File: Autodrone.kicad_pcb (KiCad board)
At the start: 4 copper layers, 37.1 x 37.2 mm, 124 parts, among them J1 Conn_01x02, J10 Conn_01x08, J11 Conn_01x03, J12 Conn_01x02, J13 USB_B_Micro, J14 Conn_01x04, J15 Conn_01x04, J16 Conn_01x01, J17 Conn_01x04, J2 Conn_01x04, J3 Conn_01x04, J4 Conn_01x03, J5 Conn_01x03, J6 Conn_01x06, J7 Conn_01x06, J8 Conn_01x04, J9 Conn_01x08, Q1 BSS138, SW1 SW_Push, U1 LP2985-3.3, U10 W25Q128JVS, U2 STM32F722RETx, U3 LP2985-3.3, U4 MP4560_QFN10, U5 MP4560_QFN10, U6 MAX7456EUI+, U7 MPU-6000, U9 BMP388, Y1 27MHz

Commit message: Lots of changes made
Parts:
- removed the C1 at (89.8, 92.0)
- removed the C16 at (89.9, 96.8)
- removed the C2 at (88.0, 96.8)
- removed the C23 at (83.3, 102.5)
- removed the C39 at (108.8, 84.1)
- removed the C40 at (100.6, 78.7)
- removed the C41 at (108.8, 82.1)
- removed the C42 at (108.8, 85.1)
- removed the C43 at (99.2, 79.6)
- removed the C44 at (97.4, 83.9)
- removed the C45 at (105.6, 94.2)
- removed the C46 at (103.0, 89.4)
- removed the D3 at (97.8, 104.8)
- removed the FB3 at (98.7, 85.3)
- removed HSE1: 8MHz, Oscillator:Oscillator_SMD_Abracon_ASE-4Pin_3.2x2.5mm
- removed the J10 at (113.2, 95.3)
- removed the J14 at (80.0, 83.7)
- removed the J2 at (104.3, 105.0)
- removed the J6 at (83.5, 92.7)
- removed the J8 at (90.1, 108.2)
- removed the L5 at (96.6, 93.4)
- removed the R21 at (97.8, 102.3)
- removed the R22 at (96.6, 98.4)
- removed the R23 at (99.3, 102.3)
- removed the R25 at (108.8, 86.1)
- removed the R26 at (96.3, 102.3)
- removed the R29 at (108.8, 87.0)
- removed the R30 at (108.8, 88.0)
- removed the R9 at (93.4, 102.3)
- added C11: 1pF, Capacitor_SMD:C_0402_1005Metric, B.Cu at (74.0, 84.5)
- added C13: 10uF, Capacitor_SMD:C_0402_1005Metric, B.Cu at (84.5, 96.2)
- added C14: 10uF, Capacitor_SMD:C_0402_1005Metric, B.Cu at (84.1, 86.5)
- added C17: 2.2uF, Capacitor_SMD:C_0402_1005Metric, F.Cu at (97.2, 87.5)
- added C20: 0.1uF, Capacitor_SMD:C_0402_1005Metric, F.Cu at (97.8, 94.6)
- added C21: 0.1uF, Capacitor_SMD:C_0402_1005Metric, F.Cu at (97.5, 90.7)
- added C22: 0.1uF, Capacitor_SMD:C_0402_1005Metric, F.Cu at (99.4, 88.8)
- added C25: 0.01uF, Capacitor_SMD:C_0402_1005Metric, B.Cu at (115.3, 88.5)
- added C27: 0.01uF, Capacitor_SMD:C_0402_1005Metric, B.Cu at (121.3, 89.9)
- added C28: 0.022uF, Capacitor_SMD:C_0402_1005Metric, B.Cu at (113.9, 91.1)
- added C29: 0.47uF, Capacitor_SMD:C_0402_1005Metric, B.Cu at (120.1, 92.1)
- added C3: 33uF, Capacitor_SMD:C_0402_1005Metric, B.Cu at (78.6, 100.0)
- added C30: 0.22uF, Capacitor_SMD:C_0402_1005Metric, B.Cu at (113.9, 89.2)
- added C31: 10uF, Capacitor_SMD:C_0402_1005Metric, F.Cu at (105.3, 82.7)
- added C33: 0.1uF, Capacitor_SMD:C_0402_1005Metric, F.Cu at (109.0, 82.2)
- added C34: 0.1uF, Capacitor_SMD:C_0402_1005Metric, F.Cu at (104.1, 90.4)
- added C36: 0.1uF, Capacitor_SMD:C_0402_1005Metric, F.Cu at (111.2, 82.2)
- added D10: YELLOW, LED_SMD:LED_0603_1608Metric, F.Cu at (74.0, 105.2)
- added D11: GREEN, LED_SMD:LED_0603_1608Metric, F.Cu at (72.6, 79.0)
- added D12: GREEN, LED_SMD:LED_0603_1608Metric, F.Cu at (72.9, 104.2)
- added D13: PURPLE, LED_SMD:LED_0603_1608Metric, F.Cu at (71.9, 103.1)
- added D6: BLUE, LED_SMD:LED_0603_1608Metric, F.Cu at (76.0, 107.3)
- added FB2: 100 @ 100 Mhz, Inductor_SMD:L_0603_1608Metric, F.Cu at (102.8, 84.5)
- added G***: LOGO, Footprints:LED, F.Cu at (76.8, 80.1)
- added G***: LOGO, Footprints:LED, F.Cu at (78.3, 102.1)
- added J1: Conn_01x03, Connector_Wire:SolderWire-0.1sqmm_1x03_P3.6mm_D0.4mm_OD1mm, F.Cu at (105.2, 78.5)
- added J11: Conn_01x02, Connector_Wire:SolderWire-0.75sqmm_1x02_P4.8mm_D1.25mm_OD2.3mm, F.Cu at (120.1, 105.7)
- added J15: Conn_01x04, Connector_Wire:SolderWire-0.1sqmm_1x04_P3.6mm_D0.4mm_OD1mm, F.Cu at (94.2, 104.7)
- added J3: Conn_01x08, Connector_JST:JST_SH_SM08B-SRSS-TB_1x08-1MP_P1.00mm_Horizontal, F.Cu at (118.8, 91.6)
- added J4: Conn_01x08, Connector_Wire:SolderWire-0.1sqmm_1x08_D0.4mm_OD1mm, F.Cu at (123.3, 91.6)
- added JP1: SolderJumper_2_Open, Jumper:SolderJumper-2_P1.3mm_Open_TrianglePad1.0x1.5mm, B.Cu at (104.4, 101.5)
- added JP2: SolderJumper_2_Open, Jumper:SolderJumper-2_P1.3mm_Open_TrianglePad1.0x1.5mm, B.Cu at (106.9, 101.5)
- added L3: Arrow, Footprints:Arrow, F.Cu at (104.3, 95.4)
- added R11: 67k, Resistor_SMD:R_0402_1005Metric, B.Cu at (118.5, 94.7)
- added R12: 75k, Resistor_SMD:R_0402_1005Metric, B.Cu at (120.1, 94.2)
- added R13: 10k, Resistor_SMD:R_0402_1005Metric, B.Cu at (121.3, 92.1)
- added R14: 1k, Resistor_SMD:R_0402_1005Metric, F.Cu at (112.3, 82.2)
- added R15: 1k, Resistor_SMD:R_0402_1005Metric, F.Cu at (113.4, 82.2)
- added R16: 1k, Resistor_SMD:R_0402_1005Metric, F.Cu at (112.9, 91.3)
- added R17: 75, Resistor_SMD:R_0402_1005Metric, F.Cu at (105.3, 81.7)
- added R18: 75, Resistor_SMD:R_0402_1005Metric, F.Cu at (110.1, 82.2)
- added R19: 589, Resistor_SMD:R_0402_1005Metric, F.Cu at (109.4, 92.3)
- added R27: 1k, Resistor_SMD:R_0402_1005Metric, B.Cu at (76.1, 76.3)
- added R31: 1k, Resistor_SMD:R_0402_1005Metric, B.Cu at (75.1, 77.4)
- added R32: 1k, Resistor_SMD:R_0402_1005Metric, B.Cu at (75.4, 105.8)
- added R36: 1k, Resistor_SMD:R_0402_1005Metric, B.Cu at (73.3, 103.8)
- added R37: 1k, Resistor_SMD:R_0402_1005Metric, B.Cu at (72.3, 102.7)
- added R8: 147k, Resistor_SMD:R_0402_1005Metric, B.Cu at (74.0, 86.8)
- added U2: MP4462, Package_DFN_QFN:DFN-10-1EP_3x3mm_P0.5mm_EP1.7x2.5mm, B.Cu at (77.0, 85.5)
- added U8: DRV8424E, Package_DFN_QFN:VQFN-24-1EP_4x4mm_P0.5mm_EP2.45x2.45mm, B.Cu at (117.0, 91.6)
- added Y2: CSTNE8M00G55Z000R0, Footprints:OSC_CSTNE8M00G55Z000R0, B.Cu at (98.7, 83.1)
- C10: renamed from C34; value 390pF -> 330pF
- C19: value 2.2uF -> 0.1uF
- C26: value 10pF -> 100uF
- C32: value 10pF -> 10uF; moved to F.Cu
- C35: value 1pF -> 0.1uF; moved to F.Cu
- C37, C38: value 10uF -> 10pF
- C4: renamed from C22; footprint Capacitor_SMD:C_0603_1608Metric -> Capacitor_SMD:C_0402_1005Metric
- C47: renamed from C15; moved to B.Cu
- C5: renamed from C29; footprint Capacitor_SMD:C_0603_1608Metric -> Capacitor_SMD:C_0402_1005Metric
- C7: renamed from C24; footprint Capacitor_SMD:C_0603_1608Metric -> Capacitor_SMD:C_0402_1005Metric
- C9: renamed from C33; value 390pF -> 330pF
- D3: renamed from D1; moved to B.Cu
- D7: value YELLOW -> RED
- D8: value GREEN -> RED
- D9: value PURPLE -> YELLOW
- FB1: moved to B.Cu
- J16: moved to F.Cu
- J17: value Conn_01x04 -> Conn_01x01; footprint Connector_Wire:SolderWire-0.1sqmm_1x04_P3.6mm_D0.4mm_OD1mm -> Connector_Wire:SolderWire-0.1sqmm_1x01_D0.4mm_OD1mm
- J5: value Conn_01x03 -> Conn_01x04; footprint Connector_Wire:SolderWire-0.1sqmm_1x03_P3.6mm_D0.4mm_OD1mm -> Connector_Wire:SolderWire-0.1sqmm_1x04_P3.6mm_D0.4mm_OD1mm
- J7: value Conn_01x06 -> Conn_01x02; footprint Connector_Wire:Connector_Wire_Solder_DJI -> Connector_Wire:SolderWire-0.75sqmm_1x02_P4.8mm_D1.25mm_OD2.3mm; moved to F.Cu
- J9: value Conn_01x08 -> Conn_01x04; footprint Connector_JST:JST_SH_SM08B-SRSS-TB_1x08-1MP_P1.00mm_Horizontal -> Connector_Wire:SolderWire-0.1sqmm_1x04_P3.6mm_D0.4mm_OD1mm
- L2: renamed from L4; moved to F.Cu
- L4: renamed from L2; value 12uH -> 6.8uH
- L5: renamed from L1; value 15uH -> 8.2uH
- R25: renamed from R6; value 2k -> 330
- R28: value 233 -> 1k; moved to B.Cu
- R33, R34: value 75 -> 1k; moved to B.Cu
- R35: value 589 -> 1k; moved to B.Cu
- R7: renamed from R24; value 93.1k -> 127k
- U1: value LP2985-3.3 -> MP4462; footprint Package_TO_SOT_SMD:SOT-23-5 -> Package_DFN_QFN:DFN-10-1EP_3x3mm_P0.5mm_EP1.7x2.5mm; moved to B.Cu
- U10: value W25Q128JVS -> MAX7456EUI+; footprint Package_SO:SOIC-8_5.23x5.23mm_P1.27mm -> JPW_Footprints:MAX7456EUI&plus_T
- U3: value LP2985-3.3 -> LD1086DT33TR; footprint Package_TO_SOT_SMD:SOT-23-5 -> Package_TO_SOT_SMD:TO-252-2; moved to B.Cu
- U4: value MP4560_QFN10 -> LP2985-1.8; footprint Package_DFN_QFN:DFN-10-1EP_3x3mm_P0.5mm_EP1.7x2.5mm -> Package_TO_SOT_SMD:SOT-23-5; moved to F.Cu
- U5: value MP4560_QFN10 -> SN74AXC4T774RSVR; footprint Package_DFN_QFN:DFN-10-1EP_3x3mm_P0.5mm_EP1.7x2.5mm -> Footprints:SN74AXC4T774RSVR; moved to F.Cu
- U6: value MAX7456EUI+ -> ICM-20948; footprint JPW_Footprints:MAX7456EUI&plus_T -> Sensor_Motion:InvenSense_QFN-24_3x3mm_P0.4mm
- U7: value MPU-6000 -> BMP280; footprint Sensor_Motion:InvenSense_QFN-24_4x4mm_P0.5mm -> Package_LGA:Bosch_LGA-8_2x2.5mm_P0.65mm_ClockwisePinNumbering
- U9: value BMP388 -> STLINK-V3MODS; footprint Footprints:BMP388 -> Footprints:STLINKV3MODS
- moved J7 43.0 mm to (120.1, 77.5), turned to 135 degrees
- moved R34 40.8 mm to (74.3, 104.8), turned to 225 degrees
- moved L1 39.7 mm to (143.2, 77.9)
- moved U9 39.0 mm to (64.9, 91.6), turned to 90 degrees
- moved D5 37.2 mm to (75.7, 75.9), turned to 135 degrees
- moved D7 35.2 mm to (74.7, 77.0), turned to 135 degrees
- moved R33 34.8 mm to (74.1, 78.4), turned to 135 degrees
- moved D9 33.2 mm to (73.7, 78.0), turned to 135 degrees
- moved J17 32.0 mm to (123.1, 100.9), turned to 90 degrees
- moved R2 28.7 mm to (75.0, 83.3), turned to 0 degrees
- moved R4 28.6 mm to (77.1, 83.3), turned to 0 degrees
- moved R6 27.7 mm to (80.1, 84.3), turned to 0 degrees
- moved J8 27.4 mm to (94.2, 108.7), turned to 0 degrees
- moved C9 26.8 mm to (74.0, 85.7), turned to 180 degrees
- moved R35 26.6 mm to (73.0, 79.4), turned to 135 degrees
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- renumbered C21 to C1, C36 to C12, C17 to C15, C18 to C16, C47 to C18, C20 to C2, C9 to C23, C10 to C24, C13 to C39, C14 to C40, C3 to C41, C4 to C42, C5 to C43, C6 to C44, C7 to C45, C8 to C46, C11 to C48, C31 to C6, C28 to C8, D6 to D1, D4 to D2, D2 to D4, FB2 to FB3, J4 to J10, J11 to J12, J12 to J13, J3 to J14, J13 to J2, J1 to J6, J15 to J8, L3 to L1, R11 to R1, R8 to R10, R10 to R2, R27 to R20, R31 to R21, R2 to R22, R3 to R23, R4 to R24, R1 to R26, R7 to R29, R13 to R3, R15 to R30, R12 to R4, R19 to R5, R17 to R6, R5 to R9, U2 to U11
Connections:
- net /Connectors/BUZ- renamed /Connectors/BUZ
- net 4V5 renamed +4V5
- net Net-(C11-Pad1) renamed /MCU/VCAP
- C1 pad 1: Net-(C21-Pad1) -> /Power/BS_5
- C1 pad 2: Net-(C21-Pad2) -> /Power/SW_5
- C10 pad 1: Net-(C34-Pad1) -> /Power/COMP_5
- C12 pad 1: Net-(C34-Pad1) -> /Power/COMP_5
- C15 pad 1: Net-(C17-Pad1) -> /Power/VIN_1V8
- C16 pad 1: Net-(C18-Pad1) -> /Power/BP_1V8
- C18 pad 1: Net-(C47-Pad1) -> +3V3
- C19 pad 1: +3V3_GYRO -> +1V8
- C2 pad 1: Net-(C20-Pad1) -> /Power/BS_9
- C2 pad 2: Net-(C20-Pad2) -> /Power/SW_9
- C26 pad 1: /MCU/HSE_IN -> +5V
- C32 pad 1: Net-(C32-Pad1) -> Net-(C31-Pad1)
- C32 pad 2: GND -> /OSD/SAG
- C35 pad 1: Net-(C33-Pad1) -> +3V3
- C37 pad 1: Net-(C37-Pad1) -> GND
- C37 pad 2: Net-(C37-Pad2) -> /OSD/CLKIN
- C38 pad 1: Net-(C37-Pad1) -> GND
- C38 pad 2: /OSD/SAG -> Net-(C38-Pad2)
- C47 pad 1: /MCU/NRST -> /Debugger/NRST
- C9 pad 1: Net-(C33-Pad1) -> /Power/COMP_9
- D1 pad 1: Net-(C21-Pad2) -> /Power/SW_5
- D2 pad 1: Net-(C20-Pad2) -> /Power/SW_9
- D5 pad 1: Net-(D5-Pad1) -> /MCU/BLUE
- D5 pad 2: /MCU/LED_BLUE -> /MCU/LED_1
- D7 pad 1: Net-(D7-Pad1) -> /MCU/RED
- D7 pad 2: +5V -> /MCU/LED_2
- D8 pad 1: Net-(D8-Pad1) -> /MCU/3V3
- D8 pad 2: +9V -> +3V3
- D9 pad 1: Net-(D9-Pad1) -> /MCU/YELLOW
- D9 pad 2: VCC -> /MCU/LED_3
- FB1 pad 1: Net-(C1-Pad1) -> /Power/VIN_3V3
- J12 pad 3: /Connectors/LED -> /Connectors/LED_STRIP
- J13 pad 1: /Connectors/I2C1_SDA -> /Connectors/I2C2_SDA
- J13 pad 2: /Connectors/I2C1_SCL -> /Connectors/I2C2_SCL
- J14 pad 3: /Connectors/UART6_RX -> /Connectors/USART6_RX
- J14 pad 4: /Connectors/UART6_TX -> /Connectors/USART6_TX
- J16 pad 1: /Connectors/SWO -> /Connectors/LIMIT1_INT
- J17 pad 1: +9V -> /Connectors/LIMIT2_INT
- J5 pad 3: /CAM -> /Connectors/USART6_TX
- J7 pad 1: +9V -> /WORM1_H
- J7 pad 2: GND -> /WORM1_L
- J8 pad 3: /Connectors/UART1_RX -> /Connectors/USART1_RX
- J8 pad 4: /Connectors/UART1_TX -> /Connectors/USART1_TX
- J9 pad 1: VCC -> +5V
- J9 pad 3: /Connectors/CURR -> /Connectors/UART5_RX_CONN
- J9 pad 4: /Connectors/UART6_RX -> /Connectors/UART5_TX_CONN
- L4 pad 1: Net-(C21-Pad2) -> /Power/SW_5
- L5 pad 1: Net-(C20-Pad2) -> /Power/SW_9
- Q1 pad 1: /MCU/BUZ-_MCU -> /MCU/BUZ_MCU
- R1 pad 2: Net-(R11-Pad2) -> /Power/FB_5
- R10 pad 1: /Barometer/I2C3_SDA -> /Barometer/I2C1_SDA
- R2 pad 2: Net-(R10-Pad2) -> /Power/FB_9
- R20 pad 2: /MCU/ADC_VSENS -> /MCU/VCC_SENSE
- R21 pad 2: /MCU/ADC_VSENS -> /MCU/VCC_SENSE
- R23 pad 2: /Connectors/I2C1_SDA -> /Connectors/I2C2_SDA
- R24 pad 2: /Connectors/I2C1_SCL -> /Connectors/I2C2_SCL
- R25 pad 2: Net-(C32-Pad1) -> Net-(R25-Pad2)
- R26 pad 1: /MCU/BUZ-_MCU -> /MCU/BUZ_MCU
- R28 pad 1: Net-(D8-Pad1) -> /MCU/1V8
- R3 pad 1: Net-(R11-Pad2) -> /Power/FB_5
- R33 pad 1: /VID -> /MCU/YELLOW
- R33 pad 2: Net-(C37-Pad1) -> GND
- R34 pad 1: GND -> /MCU/5V
- R34 pad 2: /CAM -> GND
- R35 pad 1: /OSD/XFB -> /MCU/GREEN
- R35 pad 2: Net-(C44-Pad2) -> GND
- R4 pad 1: Net-(R10-Pad2) -> /Power/FB_9
- R5 pad 1: Net-(R19-Pad1) -> /Power/FREQ_5
- R6 pad 1: Net-(R17-Pad1) -> /Power/FREQ_9
- R9 pad 1: /Barometer/I2C3_SCL -> /Barometer/I2C1_SCL
- U1 pad 1: Net-(C1-Pad1) -> /Power/SW_5
- U1 pad 2: GND -> /Power/SW_5
- U1 pad 3: Net-(C1-Pad1) -> (no net)
- U1 pad 4: Net-(C2-Pad1) -> /Power/COMP_5
- U1 pad 5: +3V3 -> /Power/FB_5
- U10 pad 1: /Flash/SPI2_CS -> (no net)
- U10 pad 2: /Flash/SPI2_MISO -> (no net)
- U10 pad 5: /Flash/SPI2_MOSI -> /OSD/CLKIN
- U10 pad 6: /Flash/SPI2_SCK -> /OSD/XFB
- U10 pad 7: +3V3 -> (no net)
- U10 pad 8: +3V3 -> /MCU/SPI2_CS
- U11 pad 10: /MCU/ADC_VSENS -> /MCU/LED_3
- U11 pad 11: (no net) -> /MCU/LED_4
- U11 pad 14: /MCU/LED_BLUE -> /Connectors/M1
- U11 pad 15: /Connectors/LED -> /Connectors/M2
- U11 pad 16: /Connectors/UART2_TX -> /Connectors/M3
- U11 pad 17: /Connectors/UART2_RX -> /Connectors/M4
- U11 pad 2: (no net) -> /Connectors/LIMIT1_INT
- U11 pad 24: /MCU/BUZ-_MCU -> (no net)
- U11 pad 25: /Connectors/M2 -> /MCU/VCC_SENSE
- U11 pad 26: /Connectors/M1 -> /Connectors/CURR_SENSE
- U11 pad 28: /Connectors/UART3_TX -> /Connectors/I2C2_SCL
- U11 pad 29: /Connectors/UART3_RX -> /Connectors/I2C2_SDA
- U11 pad 3: (no net) -> /Connectors/LIMIT2_INT
- U11 pad 33: /Flash/SPI2_CS -> /MCU/SPI2_CS
- U11 pad 34: /Flash/SPI2_SCK -> /MCU/SPI2_SCK
- U11 pad 35: /Flash/SPI2_MISO -> /MCU/SPI2_MISO
- U11 pad 36: /Flash/SPI2_MOSI -> /MCU/SPI2_MOSI
- U11 pad 37: /Connectors/UART6_TX -> /Connectors/USART6_TX
- U11 pad 38: /Connectors/UART6_RX -> /Connectors/USART6_RX
- U11 pad 39: (no net) -> /MCU/WORM1_DIR
- U11 pad 40: /Barometer/I2C3_SDA -> /MCU/WORM2_DIR
- U11 pad 41: /Barometer/I2C3_SCL -> /MCU/WORM1_PWM
- U11 pad 42: /Connectors/UART1_TX -> /MCU/WORM2_PWM
- U11 pad 43: /Connectors/UART1_RX -> (no net)
- U11 pad 46: /Connectors/SWDIO -> /Debugger/SWDIO
- U11 pad 49: /Connectors/SWCLK -> /Debugger/SWCLK
- U11 pad 50: /MCU/SPI3_CS -> (no net)
- U11 pad 51: /MCU/SPI3_SCK -> /Connectors/USART3_TX
- U11 pad 52: /MCU/SPI3_MISO -> /Connectors/USART3_RX
- U11 pad 53: /MCU/SPI3_MOSI -> /MCU/UART5_TX
- U11 pad 54: (no net) -> /MCU/UART5_RX
- U11 pad 55: /Connectors/SWO -> /Debugger/SWO
- U11 pad 56: /Connectors/M4 -> /Connectors/LED_STRIP
- U11 pad 57: /Connectors/M3 -> /MCU/BUZ_MCU
- U11 pad 58: /Connectors/I2C1_SCL -> /Connectors/USART1_TX
- U11 pad 59: /Connectors/I2C1_SDA -> /Connectors/USART1_RX
- U11 pad 61: (no net) -> /Barometer/I2C1_SCL
- U11 pad 62: (no net) -> /Barometer/I2C1_SDA
- U11 pad 7: /MCU/NRST -> /Debugger/NRST
- U11 pad 8: /Connectors/CURR -> /MCU/LED_1
- U11 pad 9: (no net) -> /MCU/LED_2
- U3 pad 1: Net-(C17-Pad1) -> GND
- U3 pad 2: GND -> +3V3
- U3 pad 3: Net-(C17-Pad1) -> /Power/VIN_3V3
- U4 pad 1: Net-(C20-Pad2) -> /Power/VIN_1V8
- U4 pad 2: Net-(C20-Pad2) -> GND
- U4 pad 3: (no net) -> /Power/VIN_1V8
- U4 pad 4: Net-(C33-Pad1) -> /Power/BP_1V8
- U4 pad 5: Net-(R10-Pad2) -> +1V8
- U5 pad 1: Net-(C21-Pad2) -> /Gyro/SPI1_CS
- U5 pad 10: Net-(C21-Pad1) -> /Gyro/ICM_MOSI
- U5 pad 2: Net-(C21-Pad2) -> /MCU/SPI1_MISO
- U5 pad 3: (no net) -> /MCU/SPI1_CS
- U5 pad 4: Net-(C34-Pad1) -> /Gyro/SPI1_MISO
- U5 pad 5: Net-(R11-Pad2) -> +3V3
- U5 pad 7: Net-(R19-Pad1) -> GND
- U5 pad 8: VCC -> GND
- U5 pad 9: VCC -> /Gyro/ICM_MISO
- U6 pad 10: /MCU/SPI3_SCK -> /Gyro/REGOUT
- U6 pad 11: /MCU/SPI3_MISO -> (no net)
- U6 pad 12: Net-(R30-Pad2) -> (no net)
- U6 pad 13: (no net) -> +1V8
- U6 pad 17: Net-(R29-Pad2) -> (no net)
- U6 pad 18: Net-(R25-Pad2) -> GND
- U6 pad 19: +3V3 -> (no net)
- U6 pad 21: +3V3 -> (no net)
- U6 pad 22: Net-(C39-Pad2) -> /Gyro/ICM_CS
- U6 pad 23: GND -> /Gyro/ICM_SCK
- U6 pad 24: +3V3 -> /Gyro/ICM_MOSI
- U6 pad 3: +3V3 -> (no net)
- U6 pad 4: GND -> (no net)
- U6 pad 5: /OSD/CLKIN -> (no net)
- U6 pad 6: /OSD/XFB -> (no net)
- U6 pad 8: /MCU/SPI3_CS -> +1V8
- U6 pad 9: /MCU/SPI3_MOSI -> /Gyro/ICM_MISO
- U7 pad 2: (no net) -> +3V3
- U7 pad 3: (no net) -> /Barometer/I2C1_SDA
- U7 pad 4: (no net) -> /Barometer/I2C1_SCL
- U7 pad 5: (no net) -> GND
- U7 pad 6: (no net) -> +3V3
- U7 pad 7: (no net) -> GND
- U7 pad 8: /Gyro/SPI1_CS -> +3V3
- U9 pad 1: +3V3 -> (no net)
- U9 pad 10: +3V3 -> (no net)
- U9 pad 2: /Barometer/I2C3_SCL -> (no net)
- U9 pad 3: GND -> (no net)
- U9 pad 4: /Barometer/I2C3_SDA -> /Debugger/SWDIO
- U9 pad 5: GND -> (no net)
- U9 pad 6: +3V3 -> /Debugger/SWO
- U9 pad 9: GND -> (no net)
- Y1 pad 3: Net-(C44-Pad2) -> Net-(C38-Pad2)
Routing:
- net +9V: track 65.3 -> 0.00 mm, vias 7 -> 0
- net +3V3: track 66.1 -> 2.02 mm, vias 27 -> 0
- net +5V: track 68.3 -> 10.1 mm, vias 5 -> 0
- net /Connectors/UART6_RX: track 52.0 -> 0.00 mm, vias 2 -> 0
- net /Connectors/UART3_RX: track 51.4 -> 0.00 mm, vias 3 -> 0
- net VCC: track 50.8 -> 0.00 mm, vias 7 -> 0
- net /Connectors/UART6_TX: track 39.1 -> 0.00 mm, vias 2 -> 0
- net /Connectors/M1: track 34.6 -> 0.00 mm, vias 3 -> 0
- net /Connectors/M2: track 33.3 -> 0.00 mm, vias 3 -> 0
- net /Connectors/UART3_TX: track 32.8 -> 0.00 mm, vias 1 -> 0
- net /Connectors/SWCLK: track 30.6 -> 0.00 mm, vias 1 -> 0
- net /Connectors/SWDIO: track 30.2 -> 0.00 mm, vias 1 -> 0
- net +4V5: track 32.1 -> 2.68 mm, vias 3 -> 0
- net /Connectors/UART1_TX: track 27.3 -> 0.00 mm, vias 1 -> 0
- net /Connectors/I2C1_SDA: track 27.3 -> 0.00 mm
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- added copper zone on PWR, net +3V3
- added copper zone on GND, net GND
- added copper zone on Signal2, net GND
- added copper zone on Signal3, net GND
- removed copper zone on In2.Cu, net +3V3
- removed copper zone on B.Cu, net +5V
- removed copper zone on B.Cu, net +9V
- removed copper zone on In1.Cu, net GND
- removed copper zone on B.Cu, net Net-(C20-Pad2)
- removed copper zone on B.Cu, net Net-(C21-Pad2)
- removed copper zone on B.Cu, net VCC
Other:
- board size 37.1 x 37.2 mm -> 54.8 x 37.2 mm
- copper layers 4 -> 6
- net class Default: clearance 0.1 -> 0.127; trace_width 0.1 -> 0.127; via_dia 0.45 -> 0.4572; via_drill 0.2 -> 0.254
- net class Oshpark added: clearance 0.127, trace_width 0.127, via_dia 0.4572, via_drill 0.254
- net class USB Data: trace_width 0.1 -> 0.127; via_dia 0.45 -> 0.4572; via_drill 0.2 -> 0.254
- rule trace_clearance: 0.1 -> 0.127
- rule trace_min: 0.1 -> 0.127
- rule via_min_drill: 0.2 -> 0.254
- rule via_min_size: 0.45 -> 0.4572
- board text added: "+5V GND BUZ"
- board text added: "+5V GND LED"
- board text added: "+5V GND RX1 TX1"
- board text added: "+5V GND RX3 TX3"
- board text added: "+5V GND RX5 TX5"
- board text added: "+5V GND RX6 TX6"
- board text added: "+9V GND CAM"
- board text added: "+9V GND TX6 VID"
- board text added: "3V3 GND"
- board text added: "4 3 2 1"
- board text added: "MOTOR 1 H L"
- board text added: "MOTOR 2 H L"
- board text added: "SDA SCL"
- board text added: "VCC +9V +5V 3V3 1V8"
- board text removed: "+3V3"
- board text removed: "+5V"
- board text removed: "+9V"
- board text removed: "3V3"
- board text removed: "4V5"
- board text removed: "5V"
- board text removed: "9V"
- board text removed: "CAM"
- board text removed: "CLK"
- board text removed: "CUR"
- board text removed: "DIO"
- board text removed: "GND"
- board text removed: "M1"
- board text removed: "M2"
- board text removed: "M3"
- board text removed: "M4"
- board text removed: "MCU"
- board text removed: "MIDN WOLFE"
- board text removed: "RX1"
- board text removed: "RX2"
- board text removed: "RX3"
- board text removed: "RX6"
- board text removed: "SCL"
- board text removed: "SDA"
- board text removed: "SWD"
- board text removed: "SWO"
- board text removed: "TX1"
- board text removed: "TX2"
- board text removed: "TX3"
- board text removed: "TX6"
- board text removed: "VCC"
- board text removed: "VID"

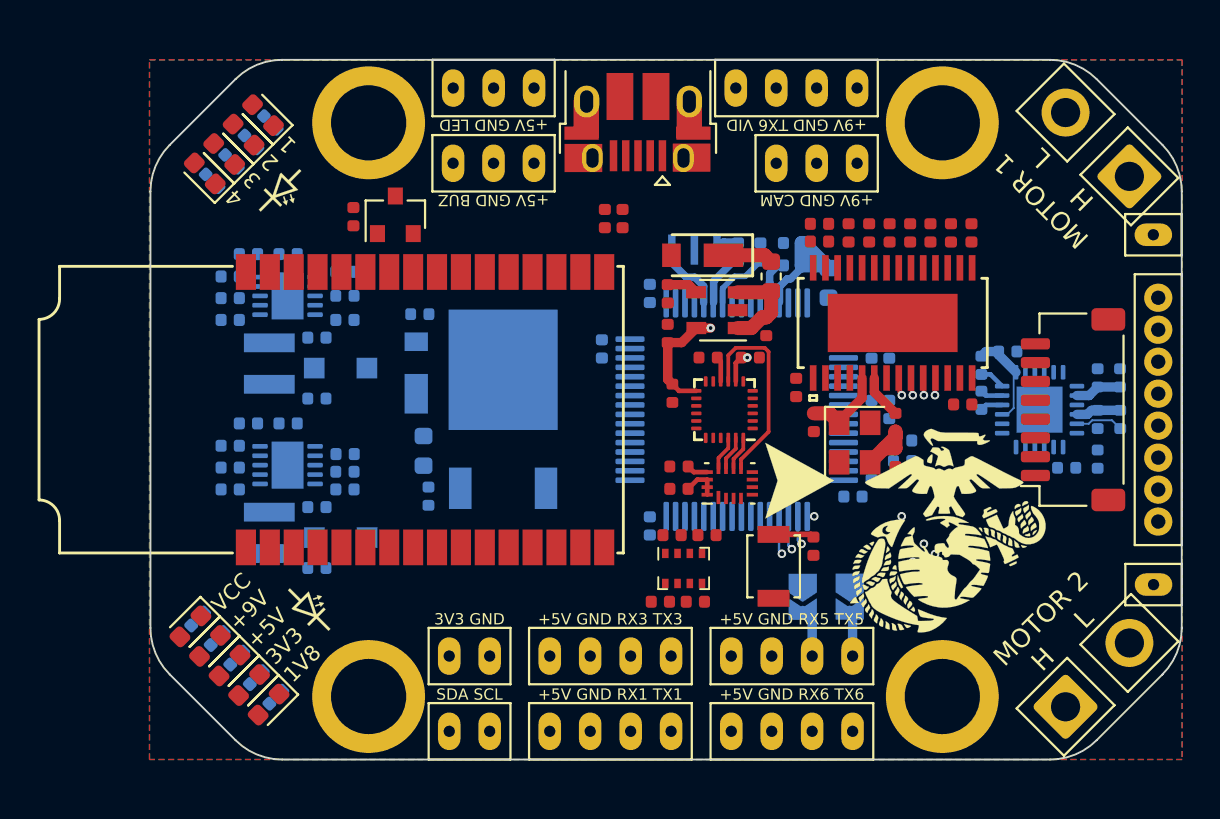
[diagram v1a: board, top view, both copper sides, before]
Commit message: Cosmetic changes to schematic
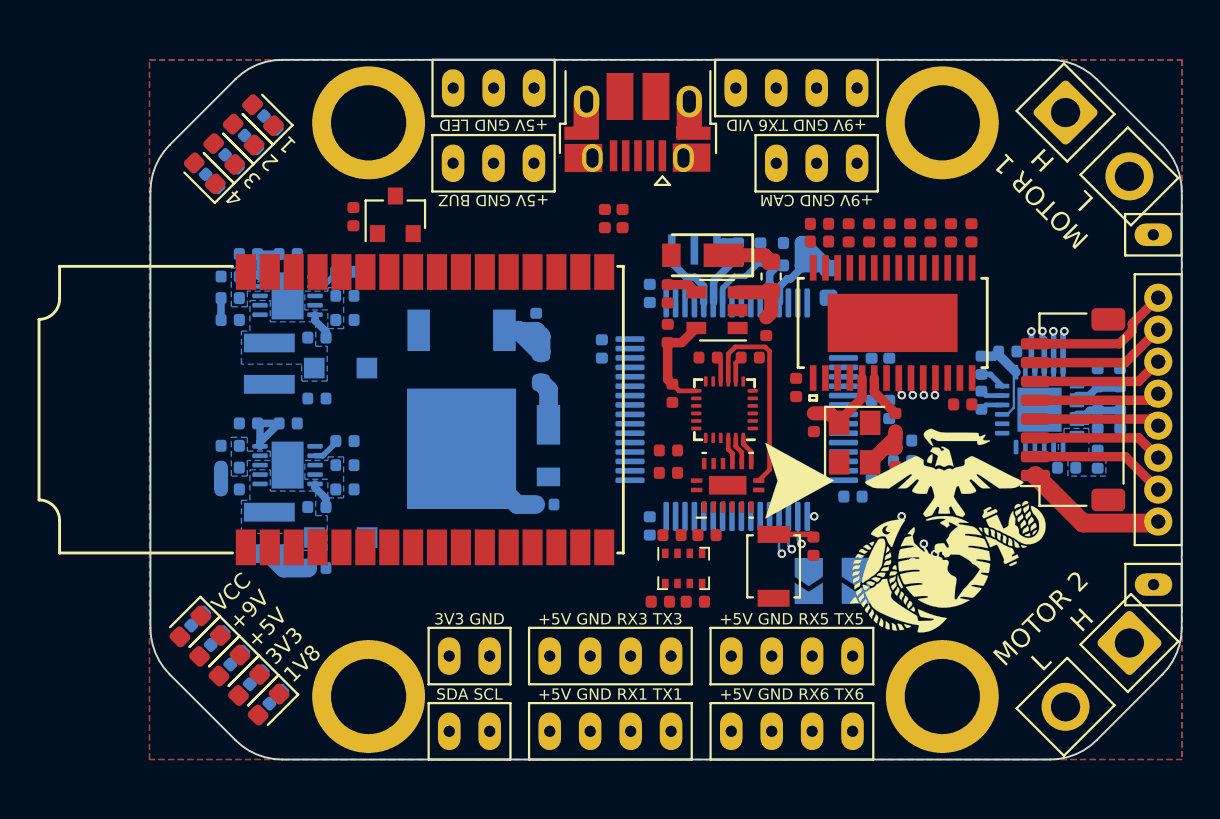
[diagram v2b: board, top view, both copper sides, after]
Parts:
- removed G*** (x2): LOGO, Footprints:LED
- removed L1: USN, Footprints:USN
- U5: value SN74AXC4T774RSVR -> SN74AXC4T774BQBR; footprint Footprints:SN74AXC4T774RSVR -> Footprints:SN74AXC4T774BQBR
- moved C14 12.1 mm to (90.7, 96.6), turned to 0 degrees
- moved C13 10.9 mm to (90.3, 87.0), turned to 90 degrees
- moved D3 8.02 mm to (90.9, 93.5), turned to 90 degrees
- moved FB1 7.65 mm to (90.5, 89.4), turned to 270 degrees
- moved U3 2.21 mm to (86.3, 91.6), turned to 270 degrees
- moved C18 1.02 mm to (97.3, 95.0)
- moved C20 1.02 mm to (97.3, 93.8)
- moved JP2 0.90 mm to (107.2, 100.7)
- moved JP1 0.90 mm to (104.8, 100.7)
- moved R5 0.69 mm to (80.1, 93.3)
- moved C5 0.35 mm to (80.1, 94.5)
- moved U5 0.15 mm to (100.4, 95.6)
- turned J11 to 225 degrees
- turned J7 to 315 degrees
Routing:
- net /WORM2_L: track 0.00 -> 22.4 mm, vias 0 -> 1
- net /WORM2_H: track 0.00 -> 20.2 mm, vias 0 -> 1
- net /WORM1_H: track 0.00 -> 14.6 mm, vias 0 -> 1
- net /WORM1_L: track 0.00 -> 12.4 mm, vias 0 -> 1
- net /Connectors/M4: track 0.00 -> 7.77 mm
- net VCC: track 0.00 -> 7.61 mm
- net GND: track 0.00 -> 7.25 mm
- net /Connectors/M3: track 0.00 -> 7.25 mm
- net /Connectors/CURR_SENSE: track 0.00 -> 6.96 mm
- net /Connectors/M2: track 0.00 -> 6.96 mm
- net /Connectors/USART6_RX: track 0.00 -> 6.67 mm
- net /Connectors/M1: track 0.00 -> 6.67 mm
- net /Power/VIN_3V3: track 0.00 -> 5.41 mm
- net +1V8: track 11.8 -> 6.96 mm, vias 2 -> 0
- net /Power/FB_9: track 0.00 -> 4.05 mm
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- added copper zone on B.Cu, net /Power/COMP_5
- added copper zone on B.Cu, net /Power/COMP_9
- added copper zone on B.Cu, net /Power/SW_5
- added copper zone on B.Cu, net /Power/SW_9
- added copper zone on B.Cu, net /WormDriver/VREF
- added copper zone on B.Cu, net VCC
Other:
- board text added: "MOTOR 1 L H"
- board text added: "MOTOR 2 L H"
- board text added: "TX1 RX1 GND +5V"
- board text added: "TX3 RX3 GND +5V"
- board text added: "TX5 RX5 GND +5V"
- board text added: "TX6 RX6 GND +5V"

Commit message: Finished routing
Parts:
- C26: footprint Capacitor_SMD:C_0402_1005Metric -> Capacitor_Tantalum_SMD:CP_EIA-3528-15_AVX-H_Pad1.50x2.35mm_HandSolder
- R10, R9: value 4.7k -> 2k2
- R23, R24: value 3.7k -> 2k2
- moved R23 24.6 mm to (86.0, 100.9), turned to 270 degrees
- moved R24 23.6 mm to (87.4, 100.9), turned to 270 degrees
- moved C26 2.54 mm to (120.3, 87.4)
- moved JP1 2.31 mm to (107.0, 101.1), turned to 0 degrees
- moved JP2 2.10 mm to (107.0, 98.6), turned to 0 degrees
- moved C46 1.80 mm to (94.5, 86.7), turned to 180 degrees
- moved C27 1.58 mm to (119.8, 90.5), turned to 0 degrees
- moved R9 1.55 mm to (98.0, 97.6), turned to 90 degrees
- moved C34 1.24 mm to (104.1, 91.7)
- moved R31 1.10 mm to (74.3, 76.6), turned to 315 degrees
- moved R27 1.10 mm to (75.3, 75.5), turned to 315 degrees
- moved R33 1.10 mm to (73.3, 77.6), turned to 315 degrees
- moved R35 1.10 mm to (72.2, 78.7), turned to 315 degrees
- moved R34 1.09 mm to (73.6, 105.6), turned to 45 degrees
- moved R36 1.09 mm to (72.5, 104.5), turned to 45 degrees
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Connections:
- J8 pad 1: +5V -> +4V5
- U11 pad 14: /Connectors/M1 -> /Connectors/M4
- U11 pad 15: /Connectors/M2 -> /Connectors/M3
- U11 pad 16: /Connectors/M3 -> /Connectors/M2
- U11 pad 17: /Connectors/M4 -> /Connectors/M1
- U11 pad 56: /Connectors/LED_STRIP -> /MCU/BUZ_MCU
- U11 pad 57: /MCU/BUZ_MCU -> /Connectors/LED_STRIP
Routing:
- net +5V: track 12.4 -> 162.3 mm, vias 0 -> 6
- net VCC: track 7.61 -> 97.3 mm, vias 0 -> 4
- net +9V: track 0.00 -> 68.0 mm, vias 0 -> 3
- net +3V3: track 5.17 -> 67.2 mm, vias 0 -> 37
- net +1V8: track 6.96 -> 52.9 mm, vias 0 -> 2
- net /Connectors/USART6_TX: track 0.00 -> 39.5 mm, vias 0 -> 1
- net /Connectors/USART6_RX: track 6.67 -> 45.5 mm, vias 0 -> 2
- net /Connectors/LIMIT2_INT: track 0.00 -> 38.7 mm, vias 0 -> 2
- net +4V5: track 5.09 -> 43.2 mm, vias 0 -> 1
- net /Connectors/I2C2_SDA: track 0.00 -> 36.8 mm, vias 0 -> 3
- net /MCU/LED_4: track 0.00 -> 36.5 mm, vias 0 -> 3
- net /Connectors/I2C2_SCL: track 0.00 -> 35.2 mm, vias 0 -> 3
- net /MCU/LED_3: track 0.00 -> 34.7 mm, vias 0 -> 3
- net /MCU/LED_2: track 0.00 -> 33.5 mm, vias 0 -> 3
- net /MCU/LED_1: track 0.00 -> 32.7 mm, vias 0 -> 3
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- added copper zone on B.Cu, net /Power/VIN_3V3

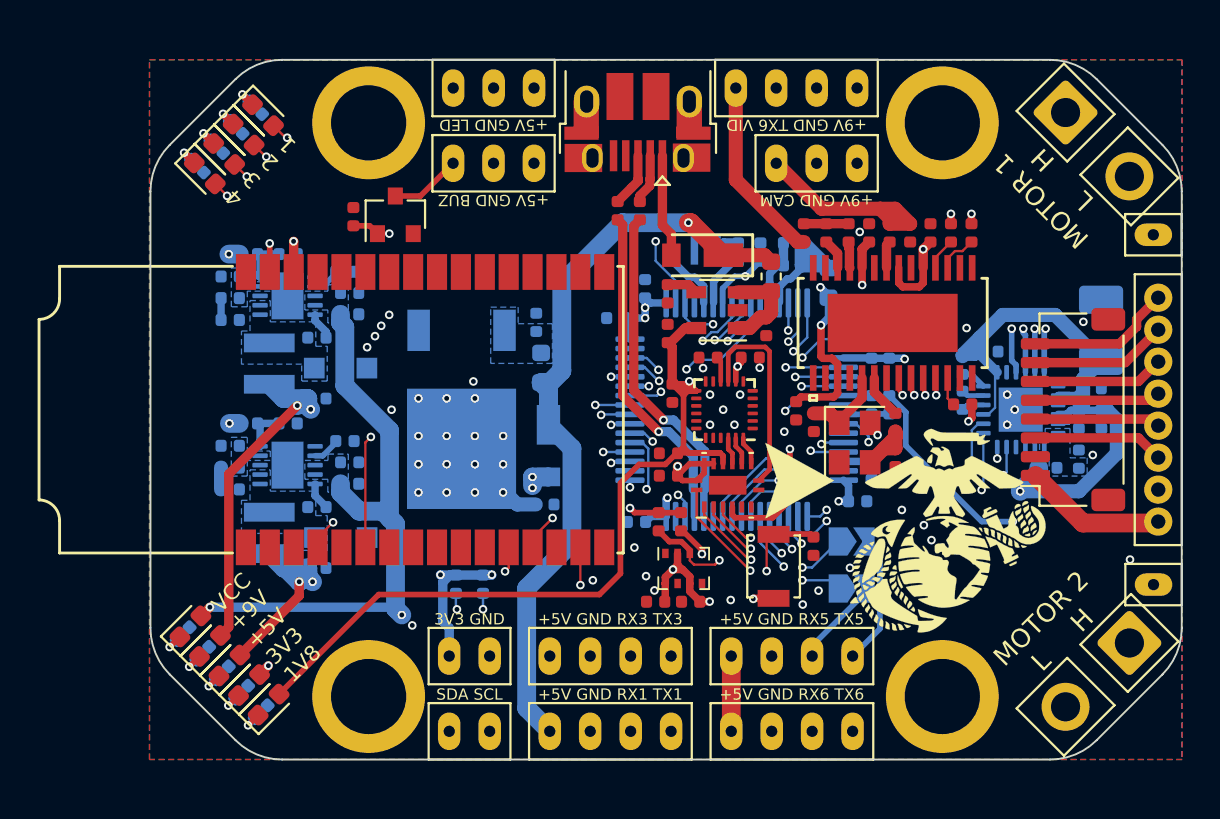
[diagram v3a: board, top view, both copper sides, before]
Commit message: Increased board size and added silkscreen text
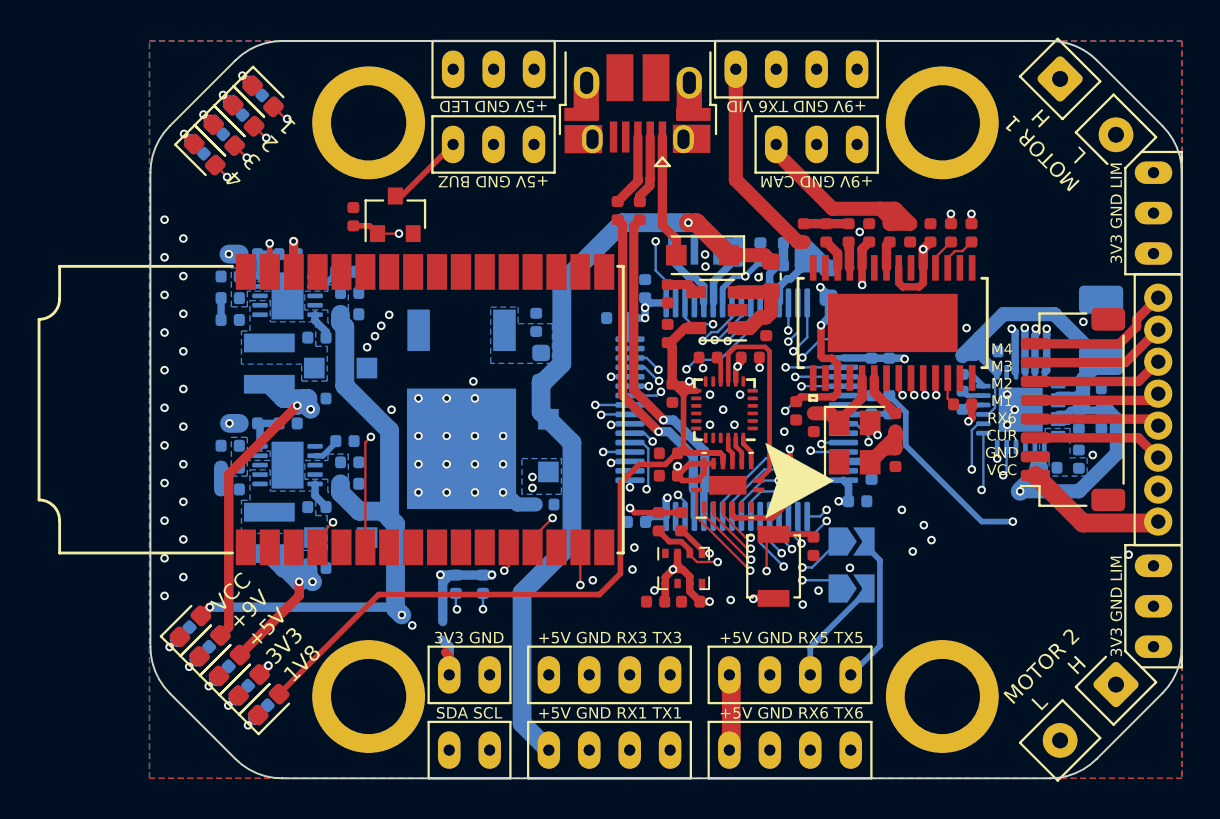
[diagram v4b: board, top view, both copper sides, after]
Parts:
- D3, D4: footprint Footprints:SBR3U30P1-7 -> Diode_SMD:D_SOD-123F
- J11, J7: footprint Connector_Wire:SolderWire-0.75sqmm_1x02_P4.8mm_D1.25mm_OD2.3mm -> Connector_Wire:SolderWire-0.25sqmm_1x02_P4.2mm_D0.65mm_OD1.7mm
- J16, J17: value Conn_01x01 -> Conn_01x03; footprint Connector_Wire:SolderWire-0.1sqmm_1x01_D0.4mm_OD1mm -> Connector_Wire:SolderWire-0.1sqmm_1x03_P3.6mm_D0.4mm_OD1mm
- L2: moved to B.Cu
- moved L2 22.6 mm to (134.7, 96.5), turned to 180 degrees
- moved J11 2.06 mm to (119.6, 107.7)
- moved J7 2.06 mm to (119.6, 75.5)
- moved J16 1.15 mm to (123.1, 81.2)
- moved J17 1.15 mm to (123.1, 102.0)
- moved J14 1.00 mm to (103.8, 109.7)
- moved J9 1.00 mm to (103.8, 105.7)
- moved J15 1.00 mm to (94.2, 105.7)
- moved J8 1.00 mm to (94.2, 109.7)
- moved D11 1.00 mm to (72.6, 78.0)
- moved D5 1.00 mm to (75.7, 74.9)
- moved D7 1.00 mm to (74.7, 76.0)
- moved D9 1.00 mm to (73.7, 77.0)
- moved J1 1.00 mm to (105.2, 77.5)
- moved J10 1.00 mm to (88.0, 77.5)
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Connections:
- J16 pad 1: /Connectors/LIMIT1_INT -> +3V3
- J17 pad 1: /Connectors/LIMIT2_INT -> +3V3
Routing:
- net +4V5: track 43.2 -> 41.0 mm
- net /VID: track 9.87 -> 11.9 mm
- net /Connectors/USART6_TX: track 39.5 -> 41.4 mm
- net /WORM2_H: track 20.9 -> 22.8 mm
- net /WORM1_L: track 12.8 -> 14.6 mm
- net /WORM2_L: track 23.1 -> 24.8 mm
- net /WORM1_H: track 15.1 -> 16.7 mm
- net /Connectors/UART5_RX_CONN: track 4.76 -> 6.34 mm
- net /Connectors/LIMIT1_INT: track 30.3 -> 31.7 mm
- net /MCU/LED_1: track 32.7 -> 34.1 mm
- net +5V_USB: track 5.49 -> 6.60 mm
- net +5V: track 162.3 -> 163.4 mm
- net /Connectors/UART5_TX_CONN: track 7.01 -> 8.05 mm
- net VCC: track 97.3 -> 98.3 mm
- net /Connectors/USART1_RX: track 21.4 -> 22.4 mm
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- added copper zone on B.Cu, net +5V
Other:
- board size 54.8 x 37.2 mm -> 54.8 x 39.2 mm
- board text added: "3V3 GND LIM"
- board text added: "AUTODRONE"
- board text added: "BUZ GND +5V"
- board text added: "CAM GND +9V"
- board text added: "GND 3V3"
- board text added: "LED GND +5V"
- board text added: "LIM GND 3V3"
- board text added: "M4 M3 M2 M1 RX6 CUR GND VCC"
- board text added: "SCL SDA"
- board text added: "TX1 RX1 GND 4V5"
- board text added: "VID TX6 GND +9V"
- board text added: "WOLFE"
- board text removed: "TX1 RX1 GND +5V"
